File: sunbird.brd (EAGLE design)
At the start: 111 x 19.1 mm, 67 parts, among them J1 USB_MINI-B_SMT, Q8010 600mA/40V, U1000 TP4056, U1500 FS312F-G, U1550 FS8205, U2000 MT3608, U2100 M3406, U4000 FM116B, U5000 CH340G, U9000 ADXL345, Y5000 12Mhz

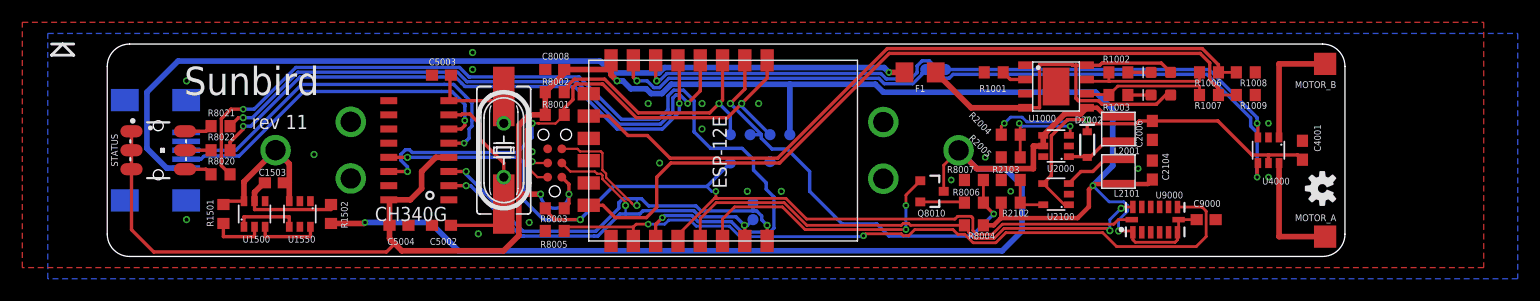
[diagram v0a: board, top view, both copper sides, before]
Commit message: Added USB-C socket. Put a copy of the RGB LED on the rear side. Rejigged components.
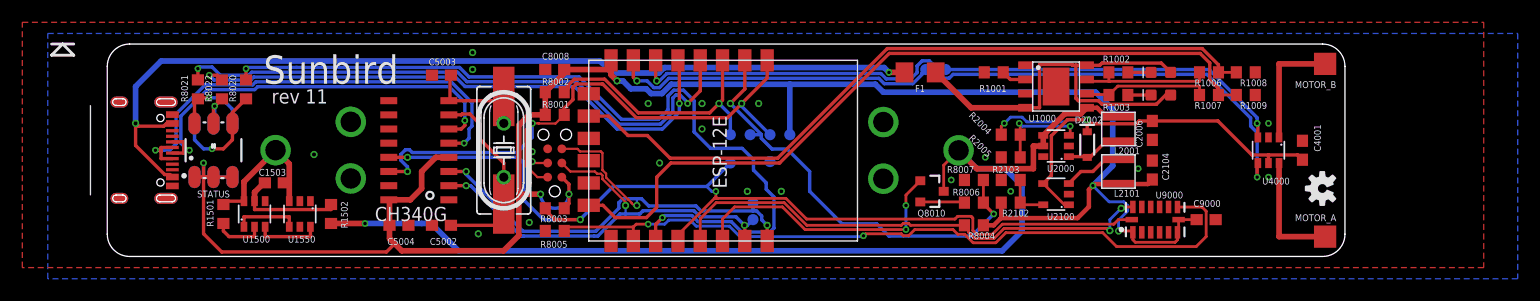
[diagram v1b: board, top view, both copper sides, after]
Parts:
- removed J1: USB_MINI-B_SMT, SparkFun-Connectors:USB-MINIB
- added STATUS1: (no value), SparkFun-LED:LED-TRICOLOR-5050
- added U$2: USB-C, geusebio:USB_C-XKBENTERPRISEU262-16XN-4BVC11
- moved R8020 7.96 mm to (12.4, 15.0), turned to 270 degrees
- moved R8022 5.46 mm to (10.3, 15.0), turned to 270 degrees
- moved STATUS 4.95 mm to (9.53, 9.53), turned to 90 degrees
- moved R8021 3.88 mm to (8.13, 15.0), turned to 270 degrees
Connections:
- removed net USB_N: J1.D-, U5000.6
- removed net USB_P: J1.D+, U5000.5
- new net D+: U$2.D+1, U$2.D+2, U5000.5
- new net D-: U$2.D-1, U$2.D-2, U5000.6
- net 3.3V: now also STATUS1.1, STATUS1.2, STATUS1.3
- net GND: now also U$2.GND1, U$2.GND2; no longer J1.GND, J1.S1, J1.S2, J1.S3, J1.S4
- net N$14: now also STATUS1.4
- net N$15: now also STATUS1.6
- net N$16: now also STATUS1.5
- net V_USB_UNFUSED: now also U$2.V+1, U$2.V+2; no longer J1.VBUS
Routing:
- net D+: track 0.00 -> 42.1 mm, vias 0 -> 2
- net D-: track 0.00 -> 37.8 mm, vias 0 -> 2
- net USB_P: track 34.0 -> 0.00 mm, vias 1 -> 0
- net USB_N: track 31.4 -> 0.00 mm, vias 1 -> 0
- net GREEN: track 83.0 -> 74.6 mm
- net N$14: track 2.53 -> 9.71 mm, vias 0 -> 1
- net V_USB_UNFUSED: track 79.2 -> 84.0 mm, vias 1 -> 2
- net N$15: track 2.53 -> 7.23 mm, vias 0 -> 1
- net BLUE: track 51.5 -> 53.9 mm
- net N$16: track 2.34 -> 4.13 mm, vias 0 -> 1
- net 3.3V: track 183.4 -> 183.2 mm, vias 5 -> 6

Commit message: documentation
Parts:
- renumbered U$1 to DEBUG
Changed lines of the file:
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@@
 <layer number="20" name="Dimension" color="24" fill="1" visible="yes" active="yes"/>
 <layer number="21" name="tPlace" color="7" fill="1" visible="yes" active="yes"/>
-<layer number="22" name="bPlace" color="7" fill="1" visible="yes" active="yes"/>
+<layer number="22" name="bPlace" color="7" fill="1" visible="no" active="yes"/>
 <layer number="23" name="tOrigins" color="15" fill="1" visible="yes" active="yes"/>
-<layer number="24" name="bOrigins" color="15" fill="1" visible="yes" active="yes"/>
+<layer number="24" name="bOrigins" color="15" fill="1" visible="no" active="yes"/>
 <layer number="25" name="tNames" color="7" fill="1" visible="yes" active="yes"/>
-<layer number="26" name="bNames" color="7" fill="1" visible="yes" active="yes"/>
+<layer number="26" name="bNames" color="7" fill="1" visible="no" active="yes"/>
 <layer number="27" name="tValues" color="7" fill="1" visible="no" active="yes"/>
 <layer number="28" name="bValues" color="7" fill="1" visible="no" active="yes"/>
@@
 <layer number="38" name="bTest" color="7" fill="1" visible="no" active="yes"/>
 <layer number="39" name="tKeepout" color="4" fill="11" visible="yes" active="yes"/>
-<layer number="40" name="bKeepout" color="1" fill="11" visible="yes" active="yes"/>
+<layer number="40" name="bKeepout" color="1" fill="11" visible="no" active="yes"/>
 <layer number="41" name="tRestrict" color="4" fill="10" visible="yes" active="yes"/>
-<layer number="42" name="bRestrict" color="1" fill="10" visible="yes" active="yes"/>
+<layer number="42" name="bRestrict" color="1" fill="10" visible="no" active="yes"/>
 <layer number="43" name="vRestrict" color="2" fill="10" visible="no" active="yes"/>
 <layer number="44" name="Drills" color="7" fill="1" visible="no" active="yes"/>
 <layer number="45" name="Holes" color="7" fill="1" visible="yes" active="yes"/>
 <layer number="46" name="Milling" color="3" fill="1" visible="no" active="yes"/>
-<layer number="47" name="Measures" color="7" fill="1" visible="yes" active="yes"/>
+<layer number="47" name="Measures" color="7" fill="1" visible="no" active="yes"/>
 <layer number="48" name="Document" color="7" fill="1" visible="no" active="yes"/>
 <layer number="49" name="Reference" color="7" fill="1" visible="no" active="yes"/>
 <layer number="50" name="dxf" color="7" fill="1" visible="no" active="no"/>
 <layer number="51" name="tDocu" color="7" fill="1" visible="yes" active="yes"/>
-<layer number="52" name="bDocu" color="7" fill="1" visible="yes" active="yes"/>
+<layer number="52" name="bDocu" color="7" fill="1" visible="no" active="yes"/>
 <layer number="53" name="tGND_GNDA" color="7" fill="9" visible="no" active="no"/>
 <layer number="54" name="bGND_GNDA" color="1" fill="9" visible="no" active="no"/>
@@
 <layer number="131" name="tAdjust" color="7" fill="1" visible="no" active="yes"/>
 <layer number="132" name="bAdjust" color="7" fill="1" visible="no" active="yes"/>
-<layer number="133" name="bottom_silk" color="7" fill="1" visible="yes" active="yes"/>
+<layer number="133" name="bottom_silk" color="7" fill="1" visible="no" active="yes"/>
 <layer number="144" name="Drill_legend" color="7" fill="1" visible="no" active="yes"/>
 <layer number="145" name="DrillLegend_01-16" color="2" fill="9" visible="no" active="yes"/>
@@
 <attribute name="VALUE" x="38.227" y="9.525" size="0.6096" layer="27" font="vector" ratio="20" rot="R90" align="top-center"/>
 </element>
-<element name="U$1" library="geusebio" package="TC2030-IDC-NL" value="ESP8266_PROGRAMMER" x="40.132" y="8.382" smashed="yes" rot="R90"/>
+<element name="DEBUG" library="geusebio" package="TC2030-IDC-NL" value="ESP8266_PROGRAMMER" x="40.132" y="8.382" smashed="yes" rot="R90"/>
 <element name="STATUS" library="SparkFun-LED" library_urn="urn:adsk.eagle:library:529" package="LED-TRICOLOR-5050" package3d_urn="urn:adsk.eagle:package:39374/1" value="" x="9.525" y="9.525" smashed="yes" rot="R90">
-<attribute name="NAME" x="9.525" y="5.9055" size="0.6096" layer="25" font="vector" ratio="20" rot="R180" align="bottom-center"/>
+<attribute name="NAME" x="12.1285" y="9.525" size="0.6096" layer="25" font="vector" ratio="20" rot="R270" align="bottom-center"/>
 <attribute name="PROD_ID" value="DIO-10298" x="9.525" y="9.525" size="1.778" layer="27" rot="R90" display="off"/>
 <attribute name="VALUE" x="12.192" y="9.525" size="0.6096" layer="27" font="vector" ratio="20" rot="R90" align="top-center"/>
 </element>
 <element name="R8020" library="rcl" library_urn="urn:adsk.eagle:library:334" package="R0603" package3d_urn="urn:adsk.eagle:package:23555/2" value="56Ohm" x="12.446" y="14.986" smashed="yes" rot="R270">
-<attribute name="NAME" x="11.557" y="13.843" size="0.6096" layer="25" rot="R90"/>
+<attribute name="NAME" x="5.715" y="14.859" size="0.6096" layer="25" rot="R90"/>
 <attribute name="SPICEPREFIX" value="R" x="12.446" y="14.986" size="1.778" layer="27" rot="R270" display="off"/>
 </element>
 <element name="R8021" library="rcl" library_urn="urn:adsk.eagle:library:334" package="R0603" package3d_urn="urn:adsk.eagle:package:23555/2" value="1Ohm" x="8.128" y="14.986" smashed="yes" rot="R270">
-<attribute name="NAME" x="7.239" y="13.843" size="0.6096" layer="25" rot="R90"/>
+<attribute name="NAME" x="4.445" y="14.859" size="0.6096" layer="25" rot="R90"/>
 <attribute name="SPICEPREFIX" value="R" x="8.128" y="14.986" size="1.778" layer="27" rot="R270" display="off"/>
 </element>
 <element name="R8022" library="rcl" library_urn="urn:adsk.eagle:library:334" package="R0603" package3d_urn="urn:adsk.eagle:package:23555/2" value="68Ohm" x="10.287" y="14.986" smashed="yes" rot="R270">
-<attribute name="NAME" x="9.398" y="13.843" size="0.6096" layer="25" rot="R90"/>
+<attribute name="NAME" x="5.08" y="14.859" size="0.6096" layer="25" rot="R90"/>
 <attribute name="SPICEPREFIX" value="R" x="10.287" y="14.986" size="1.778" layer="27" rot="R270" display="off"/>
 </element>
@@
 <element name="U$2" library="geusebio" package="USB_C-XKBENTERPRISEU262-16XN-4BVC11" value="USB-C" x="5.842" y="9.525" smashed="yes" rot="R270"/>
 <element name="STATUS1" library="SparkFun-LED" library_urn="urn:adsk.eagle:library:529" package="LED-TRICOLOR-5050" package3d_urn="urn:adsk.eagle:package:39374/1" value="" x="9.525" y="9.525" smashed="yes" rot="MR90">
-<attribute name="NAME" x="12.192" y="9.525" size="0.6096" layer="26" font="vector" ratio="20" rot="MR90" align="bottom-center"/>
 <attribute name="PROD_ID" value="DIO-10298" x="9.525" y="9.525" size="0.6096" layer="28" rot="MR90" display="off"/>
 <attribute name="VALUE" x="6.858" y="9.525" size="0.6096" layer="28" font="vector" ratio="20" rot="MR90" align="top-center"/>
@@
 <vertex x="-5.334" y="-2"/>
 </polygon>
-<contactref element="U$1" pad="6"/>
+<contactref element="DEBUG" pad="6"/>
 <via x="49.53" y="8.382" extent="1-16" drill="0.35"/>
 <via x="33.274" y="2.032" extent="1-16" drill="0.35"/>
@@
 <wire x1="40.982" y1="16.764" x2="40.982" y2="16.432" width="0.508" layer="1"/>
 <wire x1="40.982" y1="16.432" x2="39.282" y2="14.732" width="0.508" layer="1"/>
-<contactref element="U$1" pad="1"/>
+<contactref element="DEBUG" pad="1"/>
 <wire x1="41.402" y1="6.477" x2="40.767" y2="7.112" width="0.3048" layer="1"/>
 <wire x1="41.402" y1="4.738" x2="40.982" y2="4.318" width="0.3048" layer="1"/>
@@
 <wire x1="57.15" y1="2.794" x2="57.18" y2="2.764" width="0.3048" layer="1"/>
 <wire x1="57.18" y1="2.764" x2="57.18" y2="1.3895" width="0.3048" layer="1"/>
-<contactref element="U$1" pad="3"/>
+<contactref element="DEBUG" pad="3"/>
 <via x="46.482" y="4.572" extent="1-16" drill="0.35"/>
 <wire x1="46.482" y1="4.572" x2="46.482" y2="3.81" width="0.2032" layer="16"/>
@@
 <wire x1="27.35035" y1="9.3218" x2="27.09635" y2="9.5758" width="0.3048" layer="16"/>
 <wire x1="27.09635" y1="9.5758" x2="26.75165" y2="9.5758" width="0.3048" layer="16"/>
-<contactref element="U$1" pad="2"/>
+<contactref element="DEBUG" pad="2"/>
 <wire x1="38.1" y1="11.938" x2="38.6707125" y2="11.938" width="0.2032" layer="1"/>
 <wire x1="38.6707125" y1="11.938" x2="38.6873125" y2="11.9214" width="0.2032" layer="1"/>
@@
 <via x="32.1846" y="7.62" extent="1-16" drill="0.35"/>
 <wire x1="32.1846" y1="7.62" x2="30.635" y2="7.62" width="0.3048" layer="1"/>
-<contactref element="U$1" pad="5"/>
+<contactref element="DEBUG" pad="5"/>
 <wire x1="40.767" y1="9.652" x2="42.164" y2="9.652" width="0.2032" layer="1"/>
 <via x="47.498" y="4.572" extent="1-16" drill="0.35"/>
@@
 <via x="26.924" y="8.89" extent="1-16" drill="0.35"/>
 <wire x1="26.924" y1="8.89" x2="25.245" y2="8.89" width="0.3048" layer="1"/>
-<contactref element="U$1" pad="4"/>
+<contactref element="DEBUG" pad="4"/>
 <via x="38.1" y="8.509" extent="1-16" drill="0.35"/>
 <wire x1="42.418" y1="3.302" x2="40.132" y2="3.302" width="0.3048" layer="1"/>

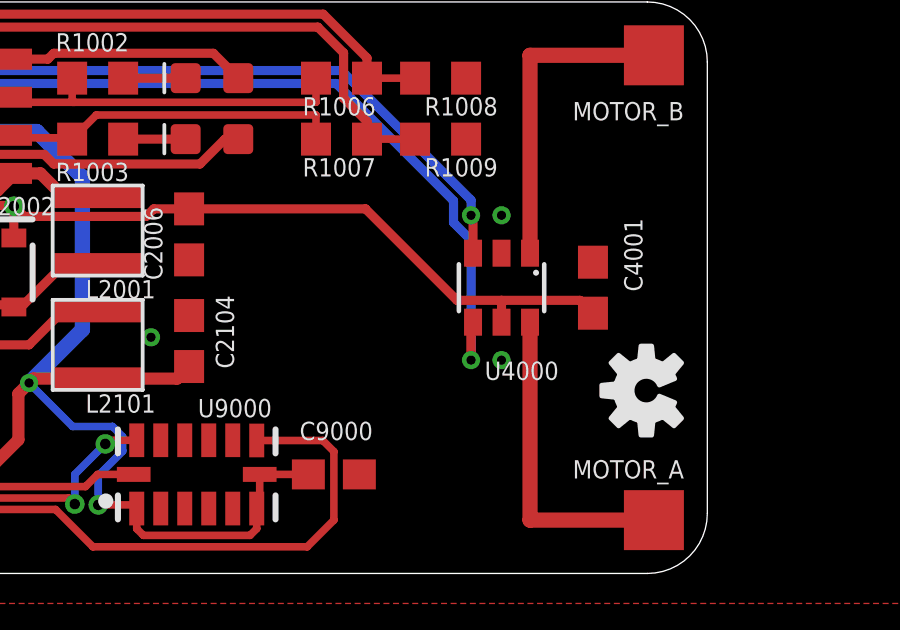
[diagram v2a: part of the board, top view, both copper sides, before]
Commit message: Add TAPR licence text to PCB silk
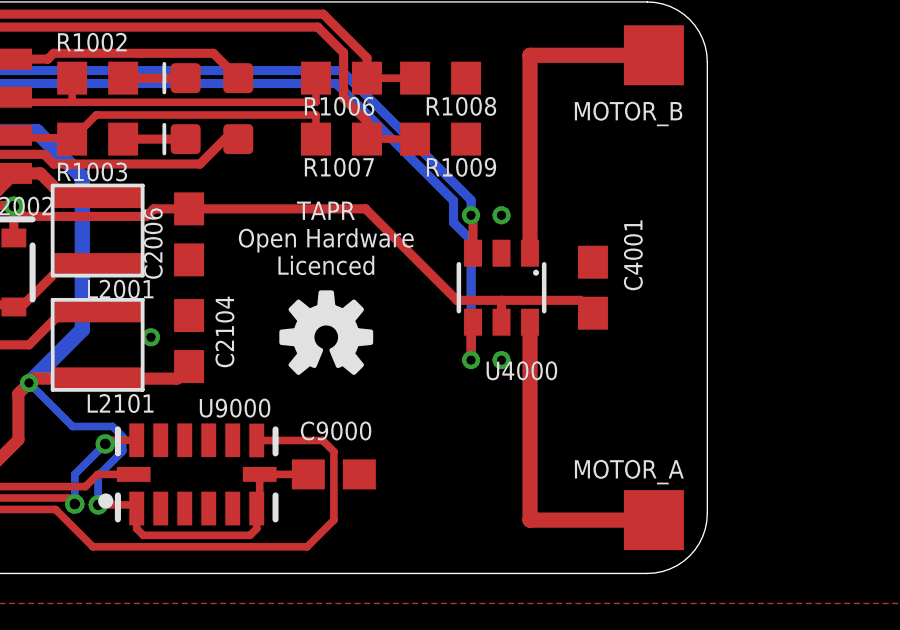
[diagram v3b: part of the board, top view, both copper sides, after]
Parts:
- moved LOGO1 10.8 mm to (98.3, 7.87), turned to 0 degrees
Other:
- board text added: "TAPR Open Hardware Licenced"
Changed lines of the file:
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@@
 <text x="-4.5" y="9.525" size="0.9" layer="47" rot="R90" align="bottom-center">19.05mm</text>
 <text x="55.5" y="-3.5" size="0.9" layer="47" align="bottom-center">111mm</text>
+<text x="98.298" y="11.176" size="0.6096" layer="25" align="center">TAPR
+Open Hardware
+Licenced</text>
 </plain>
 <attributes>
@@
 <attribute name="PROD_ID" value="RES-08585" x="72.898" y="16.51" size="1.778" layer="27" display="off"/>
 </element>
-<element name="LOGO1" library="SparkFun-Aesthetics" package="OSHW-LOGO-S" value="OSHW-LOGOS" x="108.966" y="6.096" smashed="yes" rot="R90"/>
+<element name="LOGO1" library="SparkFun-Aesthetics" package="OSHW-LOGO-S" value="OSHW-LOGOS" x="98.298" y="7.874" smashed="yes"/>
 <element name="U8000" library="ESP8266-ESP12E" package="ESP8266-ESP12E" value="" x="43.18" y="17.5895" smashed="yes" rot="R270"/>
 <element name="MOTOR_A" library="testpad" library_urn="urn:adsk.eagle:library:385" package="TP20SQ" package3d_urn="urn:adsk.eagle:package:27980/1" value="TPTP20SQ" x="109.22" y="1.778" smashed="yes">
@@
 </drawing>
 <compatibility>
+<note version="6.3" minversion="6.2.2" severity="warning">
+Since Version 6.2.2 text objects can contain more than one line,
+which will not be processed correctly with this version.
+</note>
 <note version="8.2" severity="warning">
 Since Version 8.2, EAGLE supports online libraries. The ids
